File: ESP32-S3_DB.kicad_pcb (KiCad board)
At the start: 2 copper layers, 153 parts, among them CN1 JST_Battery, IC1 SP3071EEN-L/TR, IC2 ATA6561-GAQW-N, J1 TYPE-C-31-M12_13, J10 U2RS485_TX, J11 CAN_TX, J12 CAN_RX, J14 Conn_01x06, J15 Conn_01x10, J16 Conn_01x08, J17 U2RS485_RX, J2 A - B, J3 H - L, J4 TYPE-C-31-M12_13, J5 EXT_LOAD, J6 R4_TX, J7 R4_RX, J8 Micro_SD_Card_Det1, J9 Conn_01x06, SW1 RESET, SW2 BOOT, SW3 ON/OFF, U1 ESP32-S3FH4R2, U2 UMH3N, U3 IP5306, U4 CH340X, U5 LD1117DT33CTR, X1 32.768KHz, Y1 40MHz

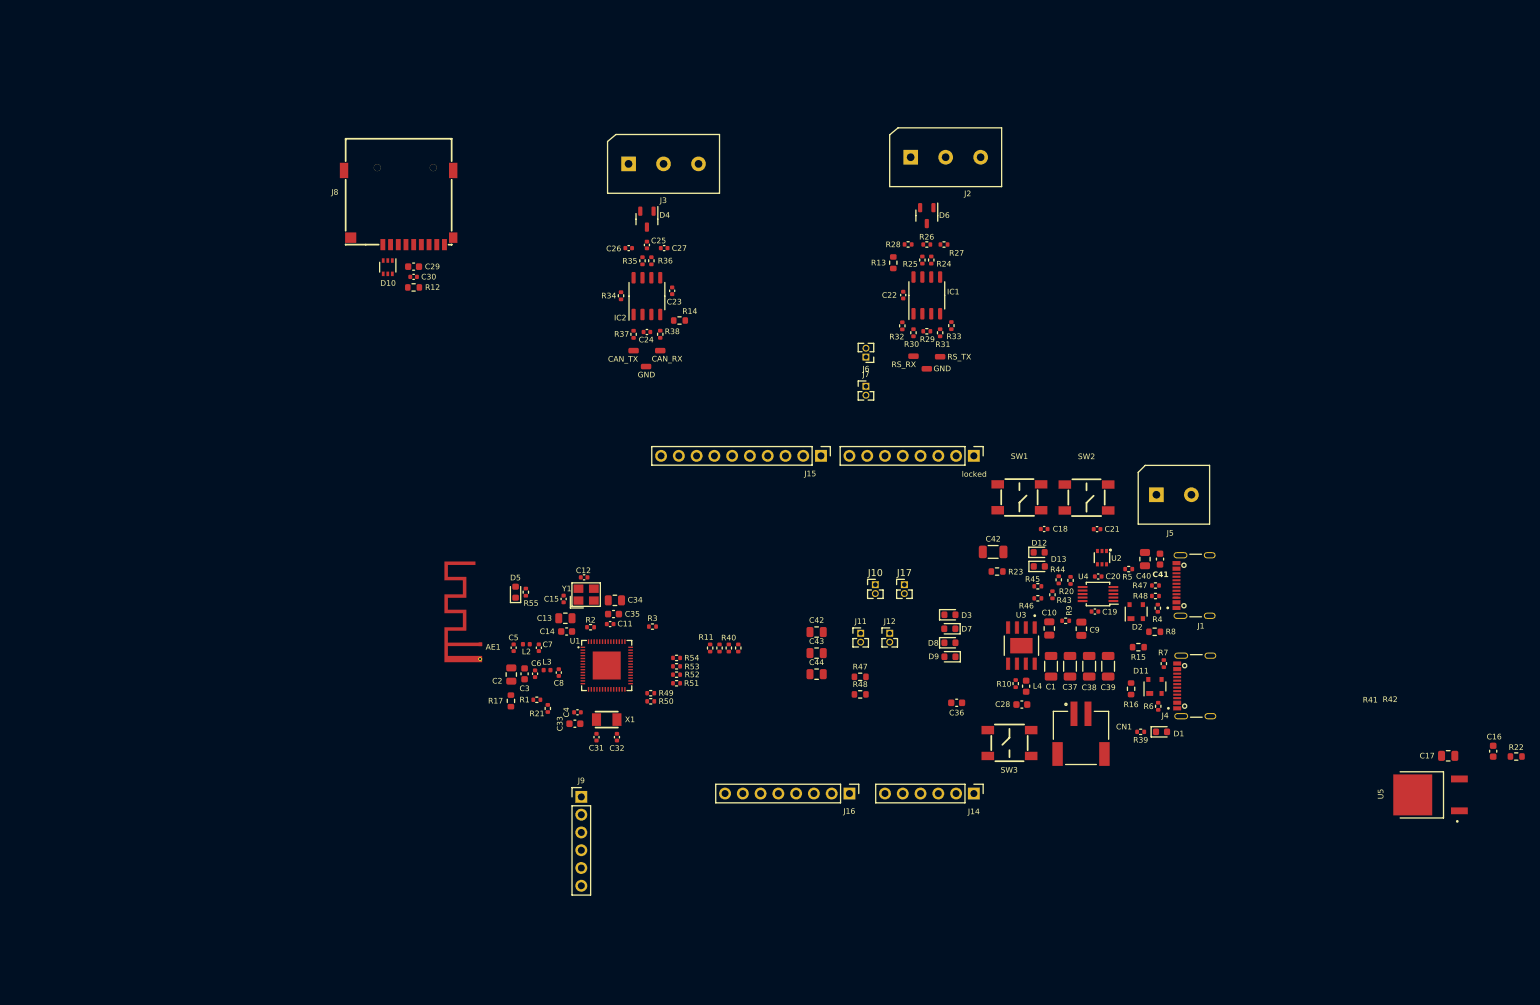
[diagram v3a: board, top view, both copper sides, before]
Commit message: Minor changes in Arduino GPIO headers
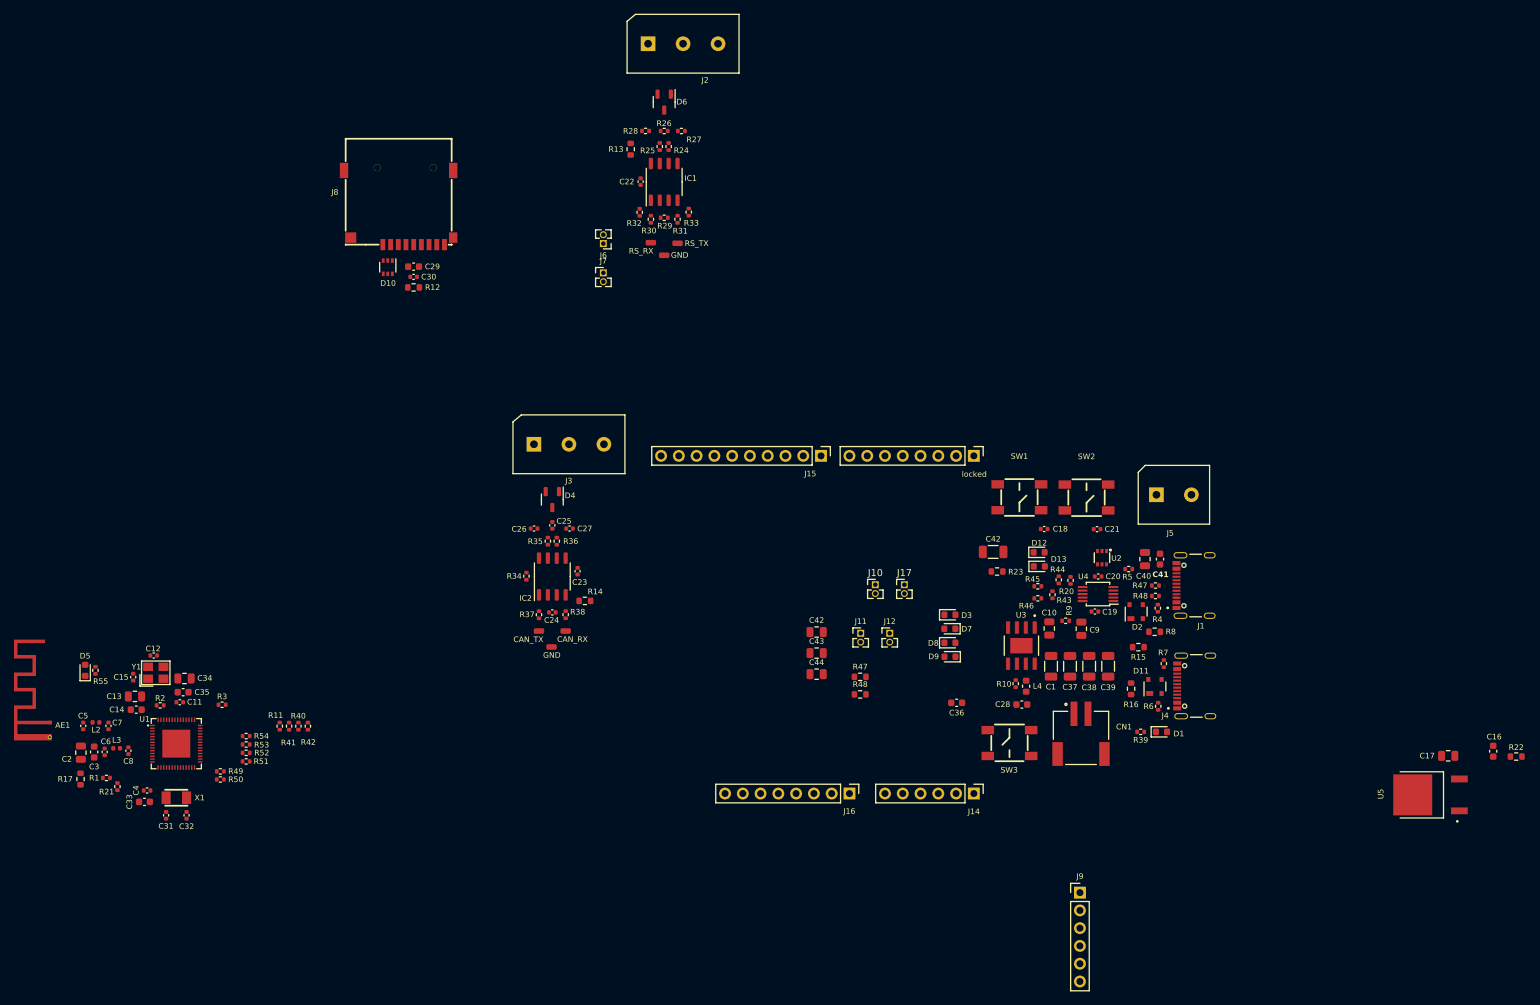
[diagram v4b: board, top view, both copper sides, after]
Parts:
- moved J9 72.6 mm to (193.1, 152.4)
- moved C31 62.5 mm to (62.5, 141.3)
- moved C8 62.5 mm to (57.1, 132.1)
- moved R21 62.5 mm to (55.6, 137.2)
- moved X1 62.5 mm to (64.0, 138.8)
- moved C13 62.5 mm to (58.1, 124.3)
- moved C15 62.5 mm to (57.8, 121.6)
- moved C3 62.5 mm to (52.2, 132.3)
- moved C32 62.5 mm to (65.5, 141.3)
- moved C33 62.5 mm to (59.4, 139.4)
- moved C34 62.5 mm to (65.2, 121.8)
- moved C35 62.5 mm to (65.0, 123.8)
- moved C5 62.5 mm to (50.7, 128.6)
- moved C6 62.5 mm to (53.8, 132.3)
- moved R1 62.5 mm to (54.0, 136.0)
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
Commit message: First draft of component layout
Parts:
- removed the C42 at (180.7, 103.7)
- removed IC1: SP3071EEN-L/TR, ESP32-S3_Dev_Board:SOP-8_3.9x4.9mm_P1.27mm
- removed the R47 at (203.9, 108.5)
- removed the R48 at (203.9, 110.0)
- added REF**: OSHW-Symbol_6.7x6mm_SilkScreen, ESP32-S3_Dev_Board:OSHW-Symbol_6.7x6mm_SilkScreen, F.Cu at (150.1, 113.2)
- added U6: SP3071EEN-L/TR, ESP32-S3_Dev_Board:SOP-8_3.9x4.9mm_P1.27mm, F.Cu at (144.9, 123.4)
- moved J2 104.9 mm to (130.3, 135.8), turned to 180 degrees
- moved R22 95.6 mm to (167.2, 96.3)
- moved C17 94.5 mm to (155.2, 105.7), turned to 180 degrees
- moved C16 93.9 mm to (161.1, 109.5), turned to 180 degrees
- moved U5 89.3 mm to (161.4, 102.6), turned to 0 degrees
- moved J9 88.9 mm to (105.4, 138.3), turned to 90 degrees
- moved D6 84.0 mm to (133.3, 123.4), turned to 0 degrees
- moved R13 82.8 mm to (140.0, 128.2), turned to 180 degrees
- moved R28 82.8 mm to (137.4, 126.1), turned to 90 degrees
- moved R26 80.0 mm to (137.4, 123.4), turned to 90 degrees
- moved R25 78.6 mm to (139.6, 124.1), turned to 180 degrees
- moved C22 77.5 mm to (145.1, 126.9), turned to 0 degrees
- moved R27 77.4 mm to (137.4, 121.0), turned to 90 degrees
- moved R24 77.2 mm to (139.6, 122.8), turned to 180 degrees
- moved J6 76.8 mm to (158.9, 128.6), turned to -90 degrees
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- renumbered IC2 to U7
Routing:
- net unconnected-(J1-SBU2-PadB8): track 0.55 -> 0.00 mm
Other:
- board outline added: 117 x 61 mm

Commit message: Added 3D Models
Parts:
- moved C29 11.7 mm to (116.7, 101.5)
- moved C30 11.7 mm to (116.7, 103.0)
- moved R12 11.7 mm to (116.7, 104.5)
- moved D10 11.5 mm to (112.8, 102.5)
- moved AE1 6.06 mm to (100.5, 126.5)
- moved C15 4.16 mm to (112.0, 111.0)
- moved C33 4.16 mm to (113.7, 128.8)
- moved C5 4.16 mm to (104.9, 118.0)
- moved C7 4.16 mm to (108.5, 118.0)
- moved L2 4.16 mm to (106.7, 117.5)
- moved X1 4.16 mm to (118.2, 128.2)
- moved C11 4.16 mm to (118.7, 114.6)
- moved C12 4.16 mm to (115.0, 107.9)
- moved C13 4.16 mm to (112.3, 113.8)
- moved C14 4.16 mm to (112.5, 115.6)
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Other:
- board size 117 x 61 mm -> 111.5 x 56.5 mm

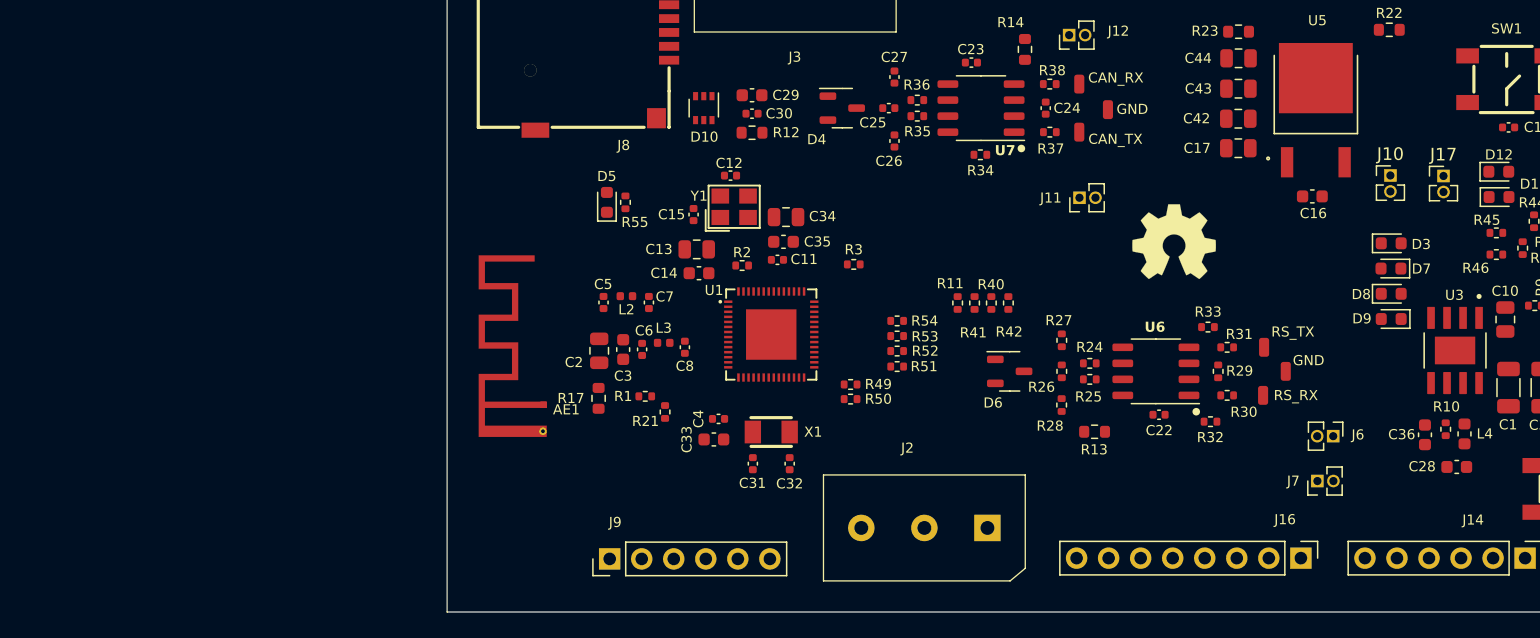
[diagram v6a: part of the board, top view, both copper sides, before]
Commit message: Added mounting holes
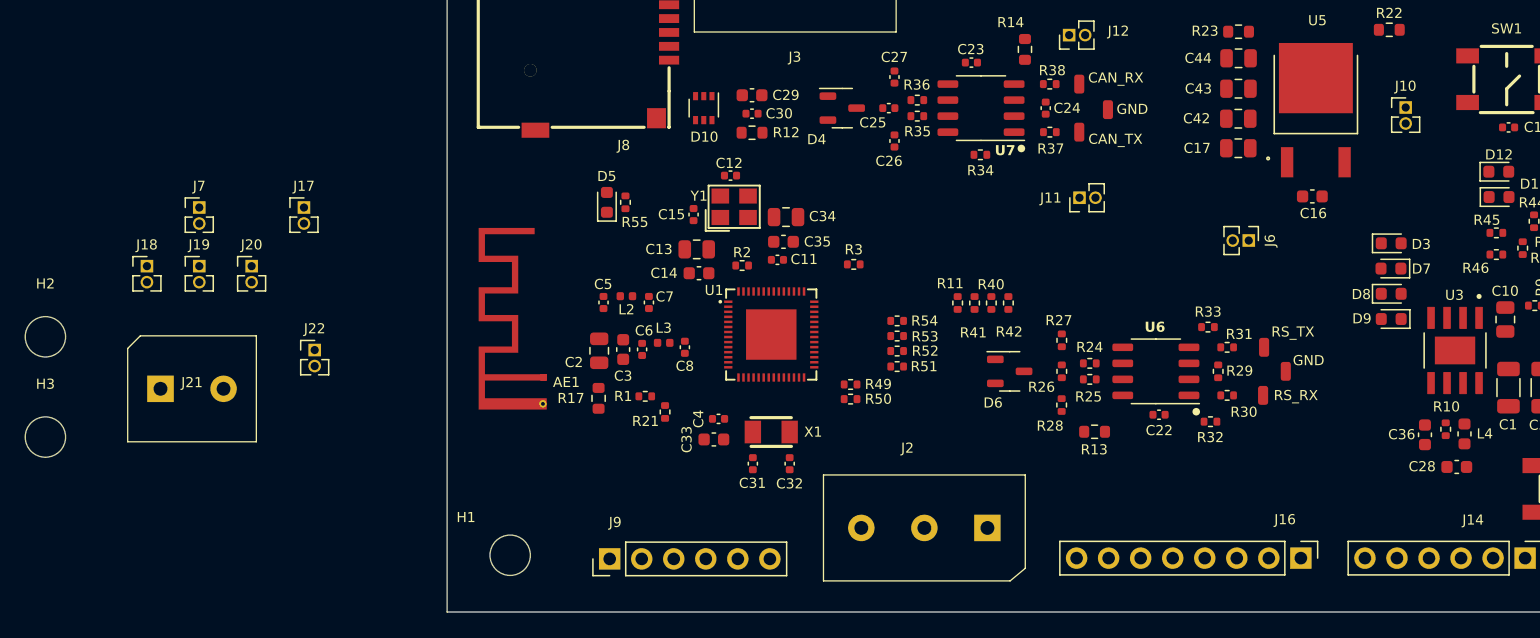
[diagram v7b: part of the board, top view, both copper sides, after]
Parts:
- removed REF**: OSHW-Symbol_6.7x6mm_SilkScreen, ESP32-S3_Dev_Board:OSHW-Symbol_6.7x6mm_SilkScreen
- added H1: MountingHole, ESP32-S3_Dev_Board:MountingHole_3.2mm_M3, F.Cu at (97.5, 138.0)
- added H2: MountingHole, ESP32-S3_Dev_Board:MountingHole_3.2mm_M3, F.Cu at (60.6, 120.7)
- added H3: MountingHole, ESP32-S3_Dev_Board:MountingHole_3.2mm_M3, F.Cu at (60.6, 128.6)
- added J18: U2RS485_DE_~{RE}, ESP32-S3_Dev_Board:PinHeader_1x02_P1.27mm_Vertical, F.Cu at (68.7, 115.1)
- added J19: U2RS485_TX, ESP32-S3_Dev_Board:PinHeader_1x02_P1.27mm_Vertical, F.Cu at (72.8, 115.1)
- added J20: U2RS485_RX, ESP32-S3_Dev_Board:PinHeader_1x02_P1.27mm_Vertical, F.Cu at (77.0, 115.1)
- added J21: U2U, ESP32-S3_Dev_Board:2P_Screw_Terminal, F.Cu at (72.3, 124.8)
- added J22: PROG_Default, ESP32-S3_Dev_Board:PinHeader_1x02_P1.27mm_Vertical, F.Cu at (82.0, 121.7)
- moved J7 91.3 mm to (72.8, 110.4), turned to 0 degrees
- moved J17 90.4 mm to (81.2, 110.4)
- moved J6 16.9 mm to (156.1, 113.0)
- moved J10 5.52 mm to (168.5, 102.5)
- moved AE1 2.17 mm to (100.5, 124.3)
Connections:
- net /485_RX renamed /485_TRANS_RX
- net /485_TX renamed /485_TRANS_TX
- J10 pad 2: /485_U2U_TX -> /U2U_RXD
- J17 pad 2: /485_U2U_RX -> /U2U_TXD
- J6 pad 2: /RS-485_TX/GPIO45 -> /RS-485_RX/GPIO46
- J7 pad 2: /RS-485_RX/GPIO46 -> /RS-485_TX/GPIO45
- R3 pad 2: /485_U2U_RX -> /U2U_RXD
- R44 pad 2: /485_U2U_TX -> /USB-TO-UART/485_TX
- R45 pad 1: /485_U2U_TX -> /USB-TO-UART/485_TX
- R46 pad 2: /485_U2U_RX -> /U2U_RXD
- U2 pad 2: /R4_~{RE}_DE -> /USB-TO-UART/DTR
- U2 pad 4: /R4_~{RE}_DE -> /USB-TO-UART/DTR
- U4 pad 8: /485_U2U_TX -> /USB-TO-UART/485_TX

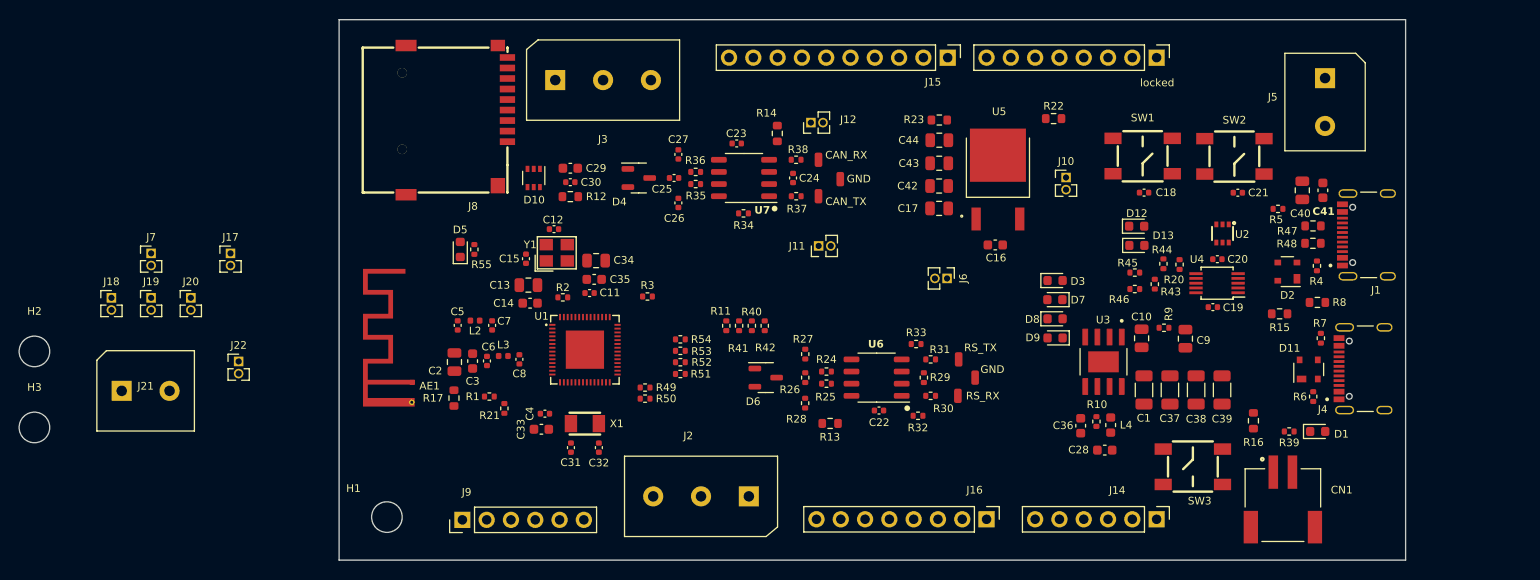
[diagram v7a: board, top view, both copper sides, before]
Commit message: Made changes in schematics, changed hierarchical sheet color
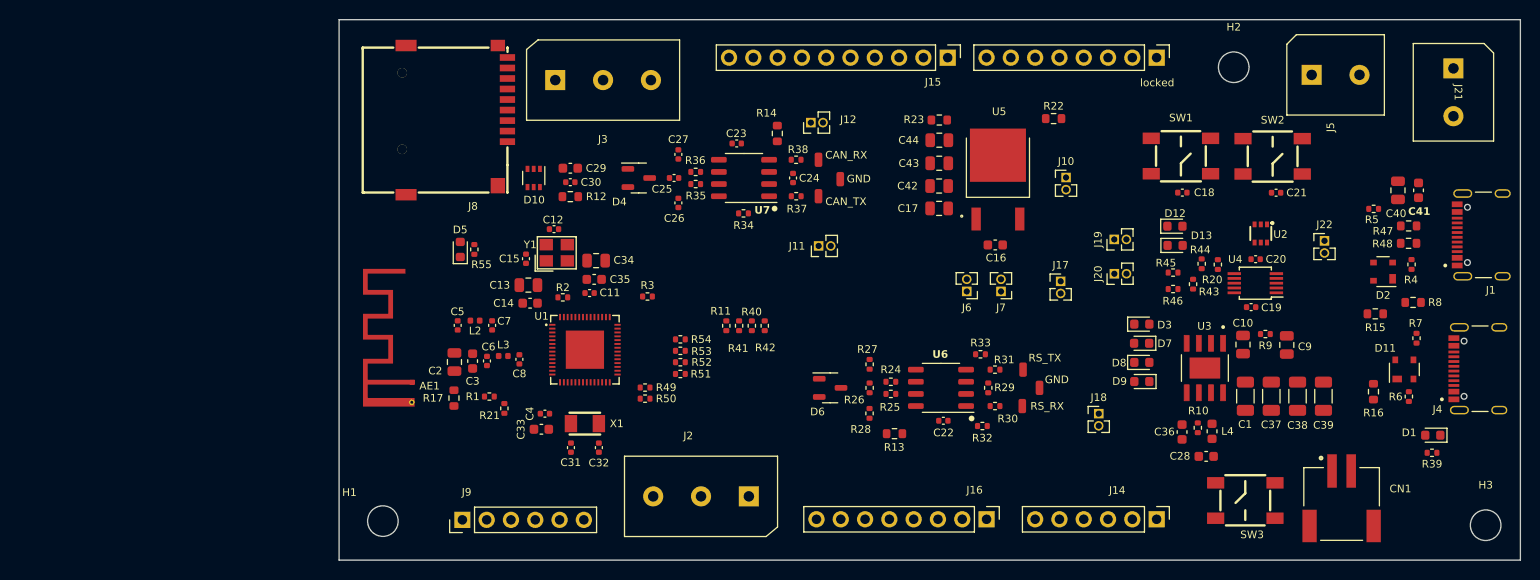
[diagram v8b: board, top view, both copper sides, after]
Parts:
- moved H3 152.1 mm to (212.4, 138.8)
- moved J21 140.2 mm to (209.0, 93.6), turned to -90 degrees
- moved H2 128.9 mm to (186.0, 91.0)
- moved J22 114.2 mm to (195.5, 109.1)
- moved J18 103.9 mm to (171.9, 127.2)
- moved J19 100.9 mm to (173.5, 109.0), turned to 90 degrees
- moved J20 96.6 mm to (173.6, 112.6), turned to 90 degrees
- moved J7 88.9 mm to (161.7, 114.4), turned to 180 degrees
- moved J17 86.8 mm to (167.9, 113.3)
- moved R39 15.1 mm to (206.8, 131.3)
- moved R16 12.9 mm to (200.6, 124.9), turned to 90 degrees
- moved D1 12.0 mm to (206.8, 129.4), turned to 180 degrees
- moved J1 12.0 mm to (214.1, 108.5)
- moved J4 12.0 mm to (213.8, 122.5)
- moved C9 10.6 mm to (191.6, 120.0)
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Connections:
- net /ESP32-S3-MCU/D+ renamed /ESP32-S3/D+
- net /ESP32-S3-MCU/D- renamed /ESP32-S3/D-
- J18 pad 2: /R4_~{RE}_DE -> /TNOW
- J22 pad 2: /R4_~{RE}_DE -> /TNOW
- R20 pad 2: /R4_~{RE}_DE -> /TNOW
- U4 pad 6: /R4_~{RE}_DE -> /TNOW
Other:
- board size 111.5 x 56.5 mm -> 123.5 x 56.5 mm
